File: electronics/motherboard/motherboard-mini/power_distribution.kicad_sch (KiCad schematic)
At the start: 54 parts, among them J8 SOLAR_CONN, J9 BATT_SHDN, U3 INA219BxD, U4 LT3652IMSE, U5 MCP73832-2-OT, U6 INA219BxD, U7 MIC2288YD5-TR, U8 XC6215B332MR-G, U9 NCP718xSN500

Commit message: added mounting circuit board and updated motherboard for next itteration
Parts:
- removed J9: BATT_SHDN, TBP02R2-381-02BE:CUI_TBP02R2-381-02BE, symbol TBP02R2-381-02BE:TBP02R2-381-02BE
- removed R27: 23K, Resistor_SMD:R_0805_2012Metric, symbol Device:R
- removed S1: DS04-254-2-02BK-SMT, DS04-254-2-02BK-SMT:SW_DS04-254-2-02BK-SMT, symbol DS04-254-2-02BK-SMT:DS04-254-2-02BK-SMT
- added BT2: 1043, 1043:BAT_1043, symbol 1043:1043
- added R? (x2): 1K, Resistor_SMD:R_0805_2012Metric, symbol Device:R
- R28: value 27K -> 10K
- R29: value 53.6K -> 21K
- R39: value 43.3K -> 47K
- R40: value 5K -> 4.7K
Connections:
- net GND: now also U9.2 (GND), BT2.N, R?.1, R?.1; no longer MOSFET1.1, MOSFET2.1
- net VBAT: now also MOSFET2.2, R37.2
- net at C11.1, R24.2, U3.7 (IN-)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: now also D5.2 (A), D6.2 (A), R29.1; no longer R25.1, R26.1
- net at U4.4 (~{CHRG}): now also R25.2; no longer D5.1 (K)
- net at U4.5 (~{FAULT}): now also R26.2; no longer D6.1 (K)
- net at BT1.P, D12.1 (K), MOSFET2.3: now also BT2.P
- new net: MOSFET1.1, R?.2
- new net: D5.1 (K), R25.1
- new net: D6.1 (K), R26.1
- new net: MOSFET2.1, R?.2
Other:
- note added: "5V (4.2 V float) Li-Ion USB Battery Charger"
- note added: "I(Reg) = 500 mA"
- note added: "R1"
- note added: "R2"
- note added: "Solar Charge IC"
- note added: "Solar Charger (12V Panels)"
- note added: "Vout = 1.24 x ((R1 / R2) + 1) Vout = 12.4 V"
- note added: "~100mA 12.4V"
- note removed: "12V Solar"
- note removed: "5V (200 mA) Li-Ion USB Battery Charger"
- note removed: "5V Solar"
- note removed: "Solar Charger (12V or 5V Panels)"
- note removed: "~100mA"
- moved on the sheet: BT1, C11, C12, C13, C14, C15, C16, C17, C18, C19, C20, C21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

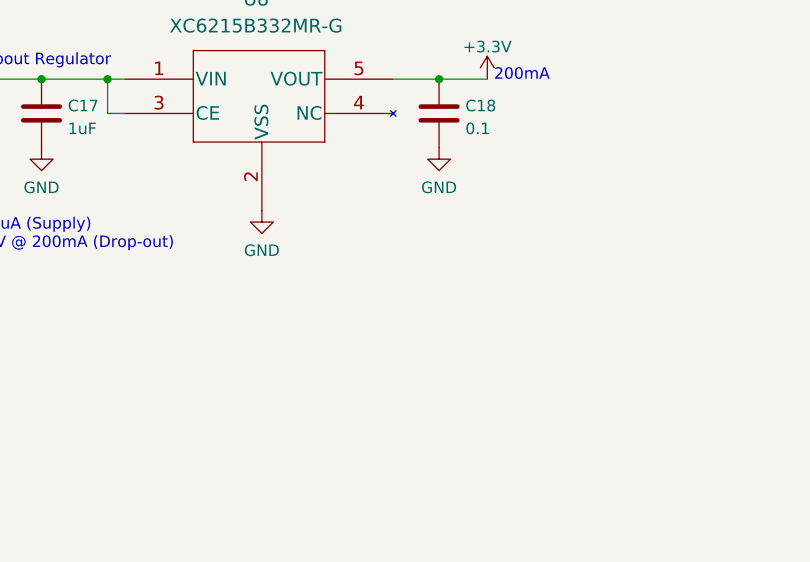
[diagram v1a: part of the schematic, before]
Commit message: first efforts with the new esp32 motherboard version
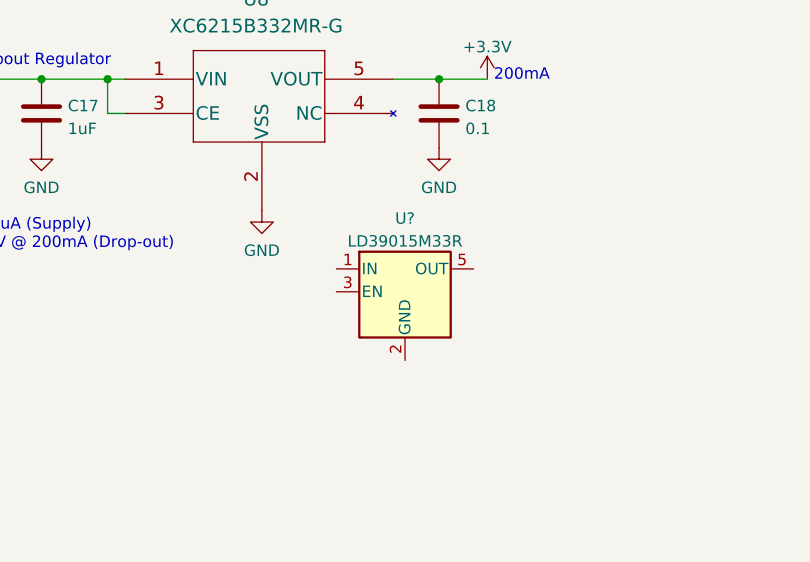
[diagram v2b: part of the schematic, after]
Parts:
- added U?: LD39015M33R, Package_TO_SOT_SMD:SOT-23-5, symbol Regulator_Linear:LD39015M33R
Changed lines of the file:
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@@
     (pin "2")
+  )
+  (symbol (lib_id "Regulator_Linear:LD39015M33R") (at 329.311 215.138 0) (unit 1)
+    (in_bom yes) (on_board yes) (fields_autoplaced)
+    (property "Reference" "U?" (id 0) (at 329.311 206.9932 0))
+    (property "Value" "LD39015M33R" (id 1) (at 329.311 209.5301 0))
+    (property "Footprint" "Package_TO_SOT_SMD:SOT-23-5" (id 2) (at 329.311 206.883 0)
+      (effects (font (size 1.27 1.27) italic) hide)
+    )
+    (property "Datasheet" "http://www.st.com/resource/en/datasheet/ld39015.pdf" (id 3) (at 329.311 215.138 0)
+      (effects (font (size 1.27 1.27)) hide)
+    )
+    (pin "1")
+    (pin "2")
+    (pin "3")
+    (pin "4")
+    (pin "5")
   )
   (symbol (lib_id "Device:R") (at 182.499 159.893 180) (unit 1)

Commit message: added cat-m1 basic interface
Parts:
- removed R? (x2): 1K, Resistor_SMD:R_0805_2012Metric, symbol Device:R
- removed U?: LD39015M33R, Package_TO_SOT_SMD:SOT-23-5, symbol Regulator_Linear:LD39015M33R
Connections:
- net GND: now also MOSFET1.1, MOSFET2.1
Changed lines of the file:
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@@
   (junction (at 215.519 209.804) (diameter 0) (color 0 0 0 0)
   )
+  (junction (at 69.342 151.003) (diameter 0) (color 0 0 0 0)
+  )
   (junction (at 263.779 191.516) (diameter 0) (color 0 0 0 0)
   )
@@
   )
   (junction (at 64.262 151.003) (diameter 0) (color 0 0 0 0)
-  )
-  (junction (at 69.342 151.003) (diameter 0) (color 0 0 0 0)
   )
   (junction (at 122.936 106.299) (diameter 0) (color 0 0 0 0)
@@
     (stroke (width 0) (type default) (color 0 0 0 0))
   )
+  (wire (pts (xy 69.342 151.003) (xy 102.616 151.003))
+    (stroke (width 0) (type default) (color 0 0 0 0))
+  )
   (wire (pts (xy 195.199 140.843) (xy 195.199 145.923))
     (stroke (width 0) (type default) (color 0 0 0 0))
@@
     (stroke (width 0) (type default) (color 0 0 0 0))
   )
-  (wire (pts (xy 69.342 151.003) (xy 102.616 151.003))
-    (stroke (width 0) (type default) (color 0 0 0 0))
-  )
   (wire (pts (xy 221.234 145.034) (xy 239.014 145.034))
     (stroke (width 0) (type default) (color 0 0 0 0))
@@
     (stroke (width 0) (type default) (color 0 0 0 0))
   )
+  (wire (pts (xy 296.291 139.446) (xy 296.291 147.066))
+    (stroke (width 0) (type default) (color 0 0 0 0))
+  )
   (wire (pts (xy 310.261 145.034) (xy 310.261 147.066))
     (stroke (width 0) (type default) (color 0 0 0 0))
@@
   )
   (wire (pts (xy 199.009 143.383) (xy 202.819 143.383))
+    (stroke (width 0) (type default) (color 0 0 0 0))
+  )
+  (wire (pts (xy 69.342 143.383) (xy 69.342 151.003))
     (stroke (width 0) (type default) (color 0 0 0 0))
   )
@@
     (pin "2")
   )
-  (symbol (lib_id "Regulator_Linear:LD39015M33R") (at 329.311 215.138 0) (unit 1)
-    (in_bom yes) (on_board yes) (fields_autoplaced)
-    (property "Reference" "U?" (id 0) (at 329.311 206.9932 0))
-    (property "Value" "LD39015M33R" (id 1) (at 329.311 209.5301 0))
-    (property "Footprint" "Package_TO_SOT_SMD:SOT-23-5" (id 2) (at 329.311 206.883 0)
-      (effects (font (size 1.27 1.27) italic) hide)
-    )
-    (property "Datasheet" "http://www.st.com/resource/en/datasheet/ld39015.pdf" (id 3) (at 329.311 215.138 0)
-      (effects (font (size 1.27 1.27)) hide)
-    )
-    (pin "1")
-    (pin "2")
-    (pin "3")
-    (pin "4")
-    (pin "5")
-  )
   (symbol (lib_id "Device:R") (at 182.499 159.893 180) (unit 1)
     (in_bom yes) (on_board yes) (fields_autoplaced)
@@
     (pin "8")
   )
-  (symbol (lib_id "Device:R") (at 69.342 147.193 180) (unit 1)
-    (in_bom yes) (on_board yes) (fields_autoplaced)
-    (property "Reference" "R?" (id 0) (at 71.12 146.3583 0)
-      (effects (font (size 1.27 1.27)) (justify right))
-    )
-    (property "Value" "1K" (id 1) (at 71.12 148.8952 0)
-      (effects (font (size 1.27 1.27)) (justify right))
-    )
-    (property "Footprint" "Resistor_SMD:R_0805_2012Metric" (id 2) (at 71.12 147.193 90)
-      (effects (font (size 1.27 1.27)) hide)
-    )
-    (property "Datasheet" "~" (id 3) (at 69.342 147.193 0)
-      (effects (font (size 1.27 1.27)) hide)
-    )
-    (pin "1")
-    (pin "2")
-  )
   (symbol (lib_id "Connector:TestPoint") (at 278.384 75.819 90) (unit 1)
     (in_bom yes) (on_board yes)
@@
       (effects (font (size 1.27 1.27)) hide)
     )
-    (pin "1")
-    (pin "2")
-  )
-  (symbol (lib_id "Device:R") (at 296.291 143.256 180) (unit 1)
-    (in_bom yes) (on_board yes) (fields_autoplaced)
-    (property "Reference" "R?" (id 0) (at 298.069 142.4213 0)
-      (effects (font (size 1.27 1.27)) (justify right))
-    )
-    (property "Value" "1K" (id 1) (at 298.069 144.9582 0)
-      (effects (font (size 1.27 1.27)) (justify right))
-    )
-    (property "Footprint" "Resistor_SMD:R_0805_2012Metric" (id 2) (at 298.069 143.256 90)
-      (effects (font (size 1.27 1.27)) hide)
-    )
-    (property "Datasheet" "~" (id 3) (at 296.291 143.256 0)
-      (effects (font (size 1.27 1.27)) hide)
-    )

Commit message: new board version sent for production, termed 'wombat' and breakout board
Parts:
- removed BT1, BT2: 1043, 1043:BAT_1043, symbol 1043:1043
- removed D10: LED(Green), LED_SMD:LED_0805_2012Metric, symbol Device:LED
- removed J8: SOLAR_CONN, TBP02R2-381-02BE:CUI_TBP02R2-381-02BE, symbol TBP02R2-381-02BE:TBP02R2-381-02BE
- removed R37: 4.7K, Resistor_SMD:R_0805_2012Metric, symbol Device:R
- added B1: 1049P, 1049P:1049P, symbol 1049P:1049P
- added F1, F2: 0685P2000-01, 0685P2000-01:0685P2000-01, symbol 0685P2000-01:0685P2000-01
- added J6, J9: 2604-3102, 2604-3102:2604-3102, symbol 2604-3102:2604-3102
- added J7: SOLAR_CRNT_JMPR, Connector_PinHeader_2.54mm:PinHeader_1x02_P2.54mm_Vertical, symbol Connector:Conn_01x02_Male
- added J8: BAT_CRNT_JMPR, Connector_PinHeader_2.54mm:PinHeader_1x02_P2.54mm_Vertical, symbol Connector:Conn_01x02_Male
- R38: value 4.7K -> 1.5K
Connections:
- net +3.3V: now also J9.1, J9.2; no longer C18.1, U8.5 (VOUT)
- net GND: now also B1.2, B1.3, J6.1, J6.2
- net at MOSFET1.3, R23.1: now also F1.2
- net at D12.1 (K), MOSFET2.3: now also F2.1
- new net: F2.2, J8.2 (Pin_2)
- new net: J6.3, J6.4, J7.2 (Pin_2)
- new net: C18.1, J9.3, J9.4, U8.5 (VOUT)
- new net: B1.1, B1.4, J8.1 (Pin_1)
- new net: F1.1, J7.1 (Pin_1)
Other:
- note added: "PWR Supply Cut-off (Switch attaches here)"
- note added: "Solar Input (12V Panels)"
- note removed: "Reverse Polarity Protection"
- note removed: "Single Cell Li-Ion 18650 (4.2 V)"
- note removed: "Solar Charger (12V Panels)"
- moved on the sheet: D4, MOSFET1, R23

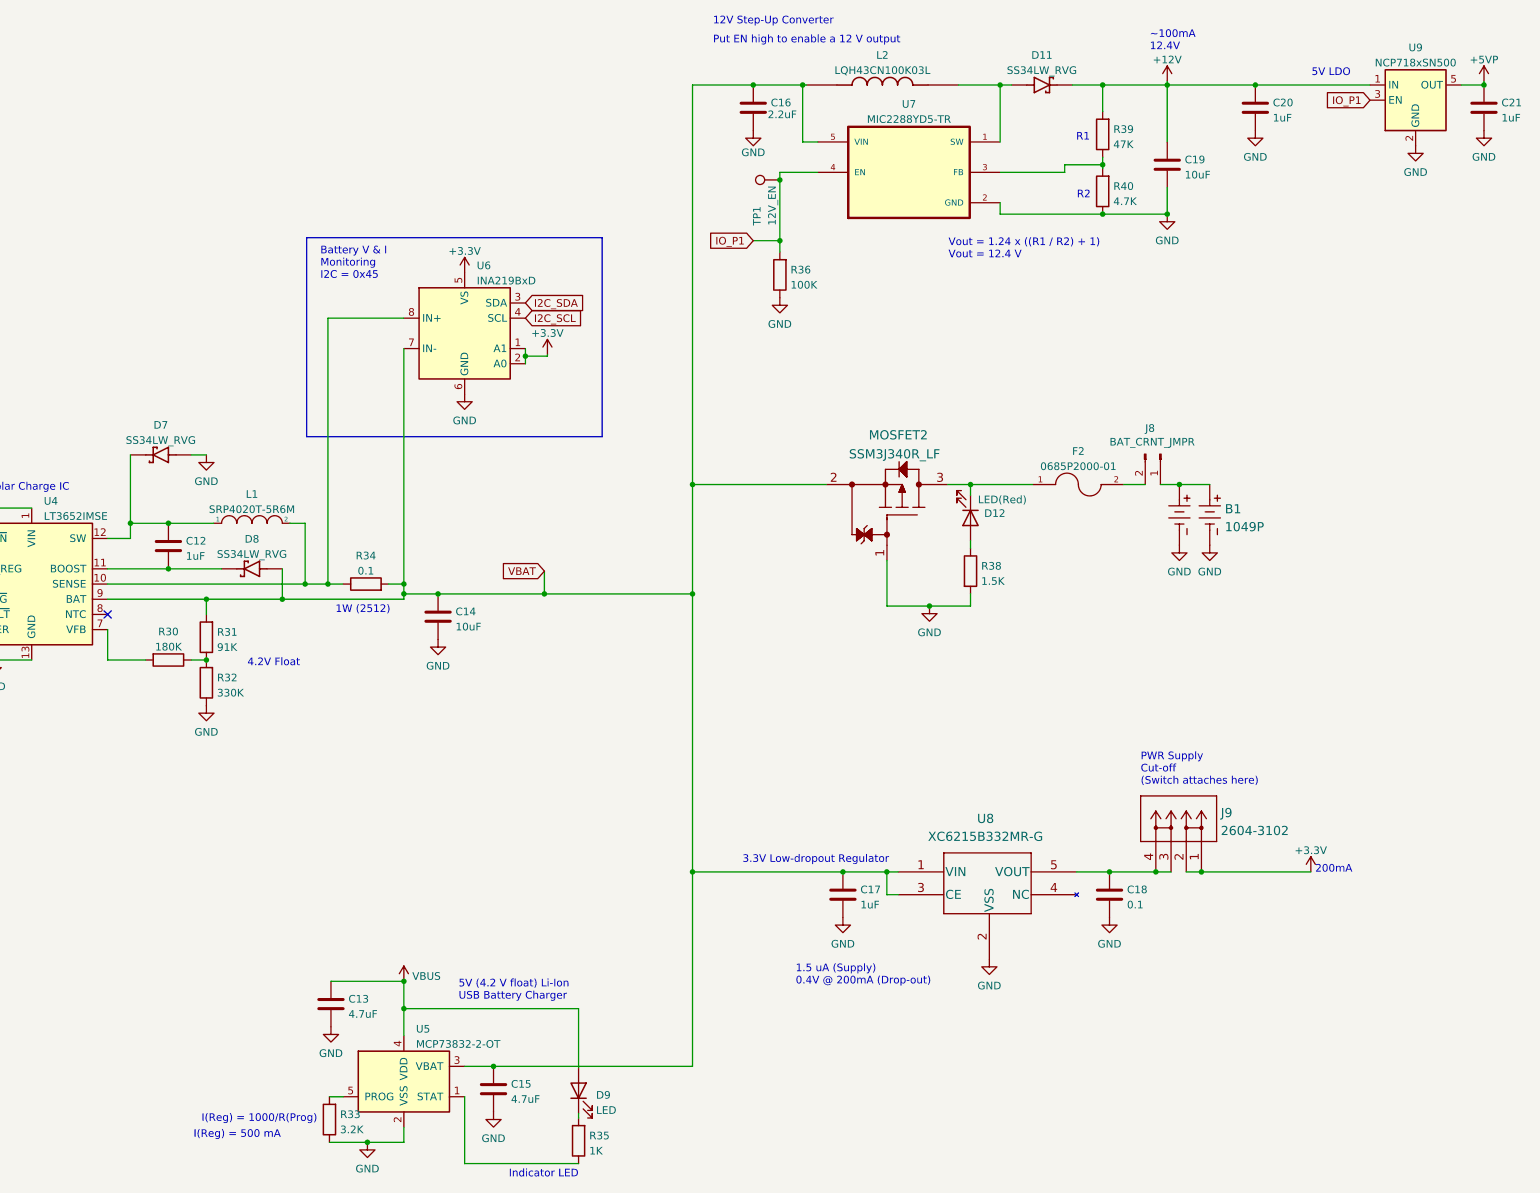
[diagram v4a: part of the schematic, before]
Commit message: added component information for all items in motherboard
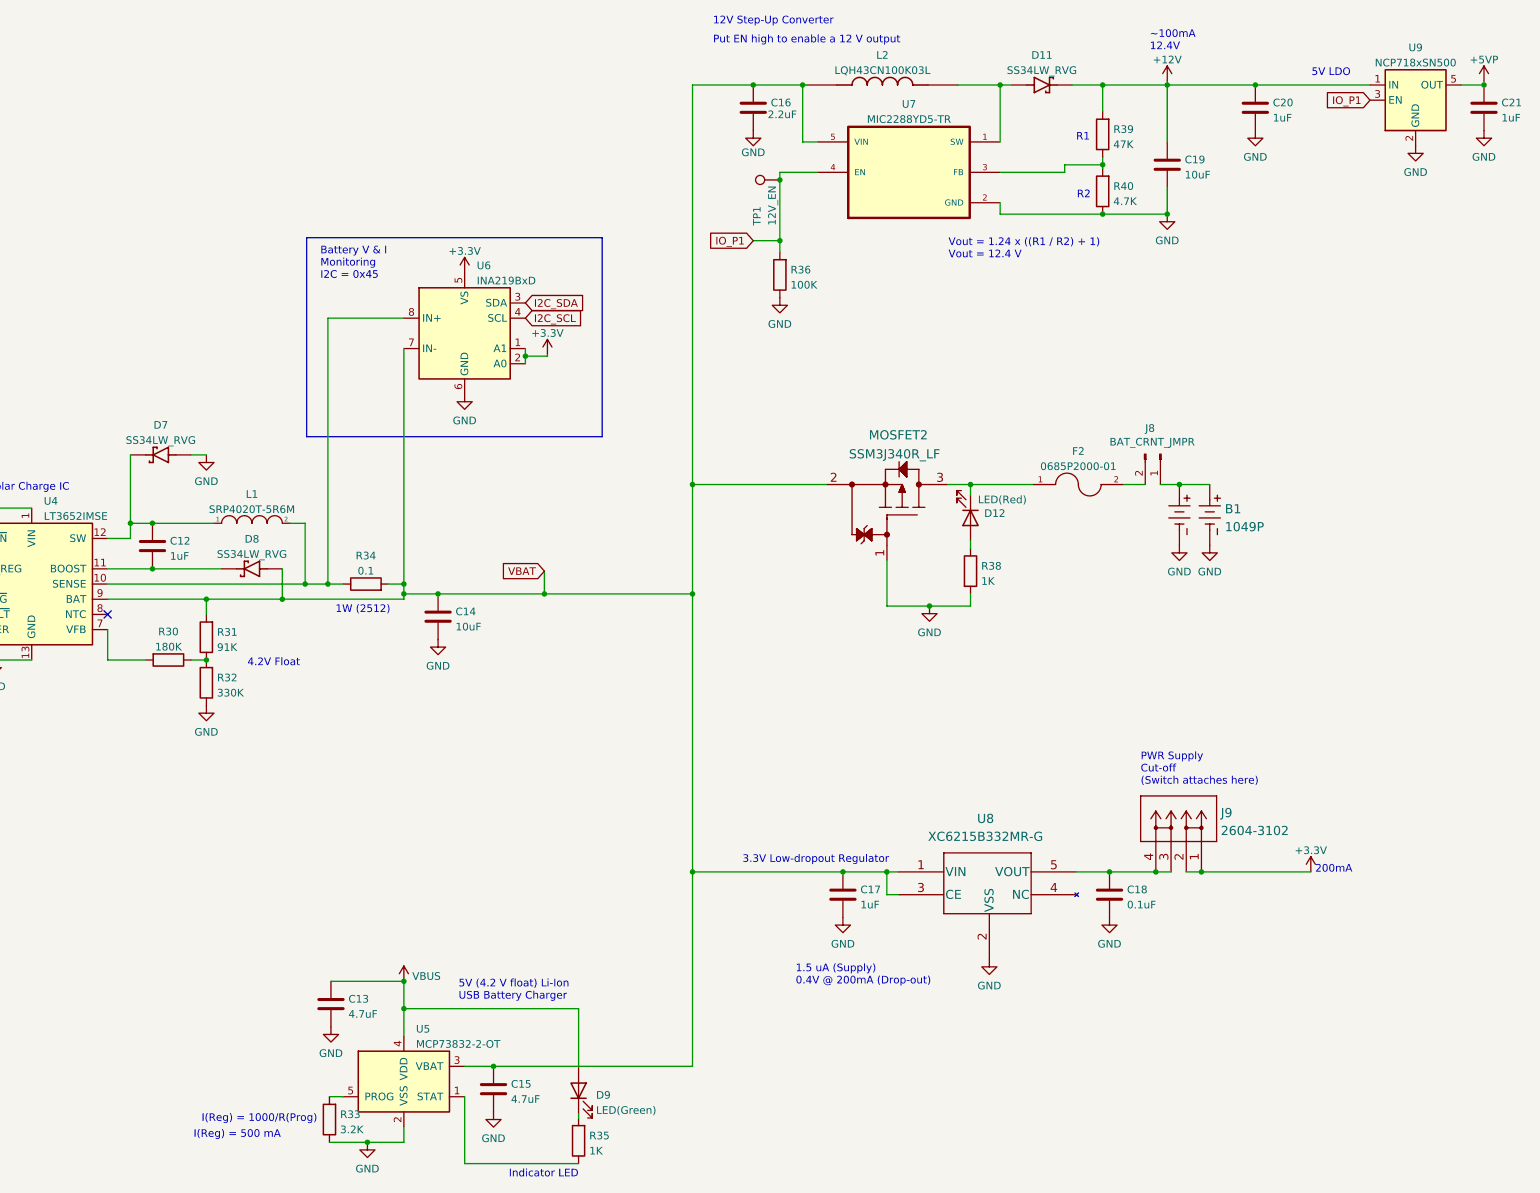
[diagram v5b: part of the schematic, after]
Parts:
- C11, C14, C19: Part (none) -> C2012X5R1V106K125AC
- C12, C17, C20, C21: Part (none) -> C0805C105K3RAC7800
- C13, C15: Part (none) -> CL21B475KOFNFNE
- C16: Part (none) -> C0805C225M3RAC7800
- C18: value 0.1 -> 0.1uF; Part (none) -> AC0805KRX7R7BB104
- D11, D7, D8: Part (none) -> SS34LW_RVG
- D12, D4, D6: Part (none) -> LS R976-NR-1
- D5: Part (none) -> LG R971-KN-1
- D9: value LED -> LED(Green); Part (none) -> LG R971-KN-1
- F1, F2: Part (none) -> 0685P2000-01
- J6, J9: Part (none) -> 2604-3102
- L1: Part (none) -> SRP4020TA-5R6M
- L2: Part (none) -> LQH43CN100K03L
- MOSFET1, MOSFET2: Part (none) -> SSM3J340R,LF
- R23, R25, R26, R40: Part (none) -> CRG0805F4K7
- R24, R34: Part (none) -> CRL2512-FW-R100ELF
- R28: Part (none) -> RC0805FR-0710KP
- R29: Part (none) -> CRCW080521K0FKEA
- R30: Part (none) -> RT0805FRE07180KL
- R31: Part (none) -> CRCW080591K0FKEA
- R32: Part (none) -> ERJ-6ENF3303V
- R33: Part (none) -> TNPW08053K20BEEA
- R35: Part (none) -> CR0805-FX-1001ELF
- R36: Part (none) -> CRCW0805100KJNTA
- R38: value 1.5K -> 1K
- R39: Part (none) -> CRCW080547K0FKTA
- U3, U6: Part (none) -> INA219BIDR
- U4: Part (none) -> LT3652IMSE
- U5: Part (none) -> MCP73832-2ATI/MC
- U7: MANUFACTURER Microchip -> (none); MAXIMUM_PACKAGE_HEIGHT 1.0mm -> (none); PARTREV B -> (none); Part (none) -> MIC2288YD5-TR; SNAPEDA_PACKAGE_ID 8798 -> (none); STANDARD IPC-7351B -> (none)
- U8: Part (none) -> XC6215B332MR-G
- U9: Part (none) -> NCP718ASN500T1G
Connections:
- net +12V: now also C20.2; no longer C20.1
- net +5VP: now also C21.2; no longer C21.1
- net GND: now also C17.1, C20.1, C21.1; no longer C17.2, C20.2, C21.2
- net VBAT: now also C17.2; no longer C17.1
- net at D8.C, U4.11 (BOOST): now also C12.1; no longer C12.2
- net at D7.C, L1.1, U4.12 (SW): now also C12.2; no longer C12.1

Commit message: updated usb-to-uart, fixed some pin label issues
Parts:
- added C?: 100uF, T520B107M006ATE015:CAPPM3528X210N, symbol T520B107M006ATE015:T520B107M006ATE015
- added C?: 1uF, Capacitor_SMD:C_0805_2012Metric, symbol Device:C
- added TP?: VOUT, TestPoint:TestPoint_Pad_D1.0mm, symbol Connector:TestPoint
- added U?: TPS22967DSGR, TPS22967DSGR:SON50P200X200X80-9N, symbol TPS22967DSGR:TPS22967DSGR
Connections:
- net GND: now also C?.1, C?.2, U?.5 (GND)
- net IO_P1: no longer R36.2, TP1.1, U7.4 (EN)
- net VBAT: now also C?.2, U?.1 (VIN), U?.2 (VIN-1), U?.4 (VBIAS); no longer C16.1, L2.1, U7.5 (VIN)
- new net: C16.1, C?.1, L2.1, TP?.1, U7.5 (VIN), U?.7 (VOUT), U?.8 (VOUT-1)
- new net IO_P6: R36.2, TP1.1, U7.4 (EN), U?.3 (ON)
- no-connect marks 1 -> 2
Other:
- note added: "Power Shutoff"
- moved on the sheet: B1, C11, C12, C13, C14, C15, C16, C17, C18, C19, C20, C21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
